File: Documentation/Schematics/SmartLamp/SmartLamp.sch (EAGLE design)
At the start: 31 parts, among them J1 POWER_JACKPTH_BREAD, J2 AVR_SPI_PROG_5X2PTH2, Q1 STN4NF03L, Q2 STN4NF03L, Q3 STN4NF03L, U1 MIC2920A, U2 DS3231MZ, U3 ATMEGA8/168/328, U4 HM-10

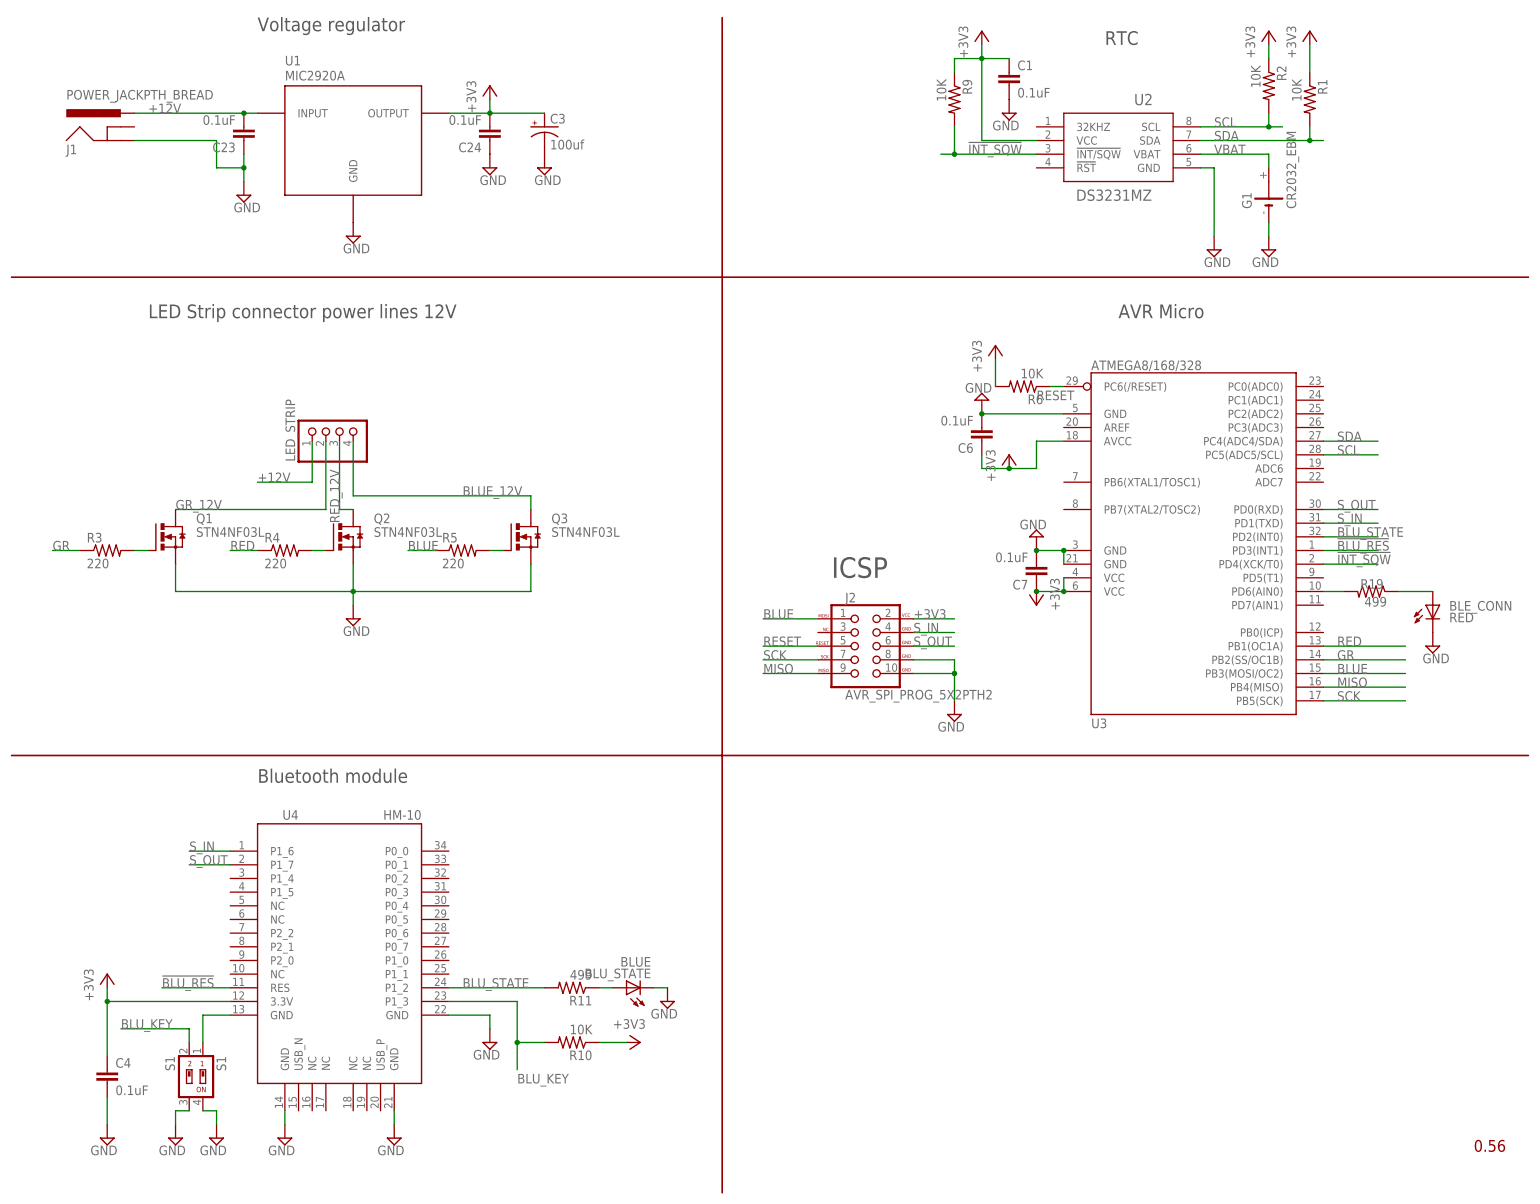
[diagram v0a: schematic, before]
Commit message: Arranged label with smashed part on schematic and board
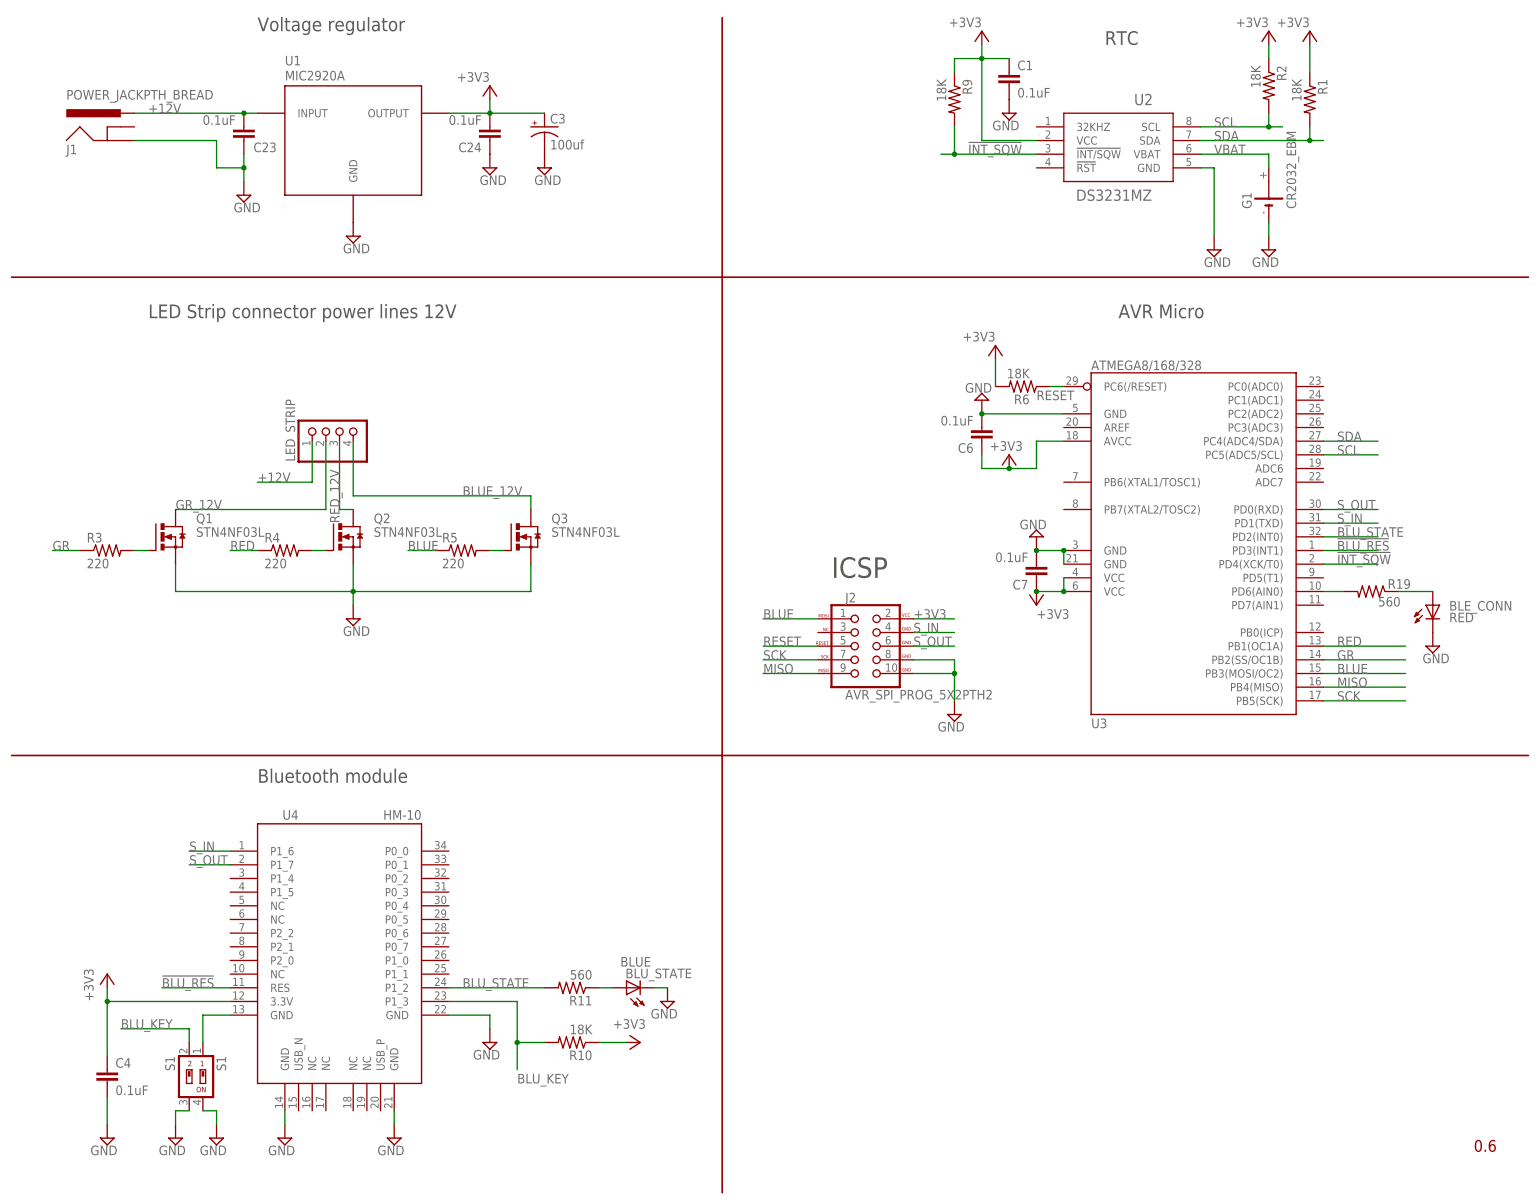
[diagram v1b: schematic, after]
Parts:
- R1, R10, R2, R6, R9: value 10K -> 18K
- R11, R19: value 499 -> 560
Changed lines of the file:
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@@
 <schematic xreflabel="%F%N/%S" xrefpart="/%S.%C%R">
 <attributes>
-<attribute name="VERSION" value="0.56"/>
+<attribute name="VERSION" value="0.6"/>
 </attributes>
 <variantdefs>
@@
 </classes>
 <parts>
-<part name="R2" library="rcl" deviceset="R-US_" device="R1206" value="10K"/>
-<part name="R1" library="rcl" deviceset="R-US_" device="R1206" value="10K"/>
+<part name="R2" library="rcl" deviceset="R-US_" device="R1206" value="18K"/>
+<part name="R1" library="rcl" deviceset="R-US_" device="R1206" value="18K"/>
 <part name="GND4" library="supply2" deviceset="GND" device=""/>
 <part name="J1" library="SparkFun-Connectors" deviceset="POWER_JACK" device="PTH_BREAD"/>
@@
 <part name="G1" library="CuSTOM_GB" deviceset="CR2032_EBM" device=""/>
 <part name="U2" library="Maxim_RTC" deviceset="DS3231MZ" device=""/>
-<part name="R9" library="rcl" deviceset="R-US_" device="R1206" value="10K"/>
+<part name="R9" library="rcl" deviceset="R-US_" device="R1206" value="18K"/>
 <part name="FRAME2" library="frames" deviceset="DOCFIELD" device=""/>
 <part name="SUPPLY52" library="supply2" deviceset="GND" device=""/>
@@
 <part name="Q2" library="transistor-power" deviceset="N-HEXFET-2D_?-*" device="SOT232" technology="IRLL014N" value="STN4NF03L"/>
 <part name="Q3" library="transistor-power" deviceset="N-HEXFET-2D_?-*" device="SOT232" technology="IRLL014N" value="STN4NF03L"/>
-<part name="R6" library="rcl" deviceset="R-US_" device="R1206" value="10K"/>
+<part name="R6" library="rcl" deviceset="R-US_" device="R1206" value="18K"/>
 <part name="+3V1" library="supply1" deviceset="+3V3" device=""/>
 <part name="C3" library="SparkFun-Capacitors" deviceset="CAP_POL" device="C" value="100uf"/>
@@
 <part name="SUPPLY20" library="supply2" deviceset="GND" device=""/>
 <part name="SUPPLY9" library="supply2" deviceset="GND" device=""/>
-<part name="R19" library="rcl" deviceset="R-US_" device="R1206" value="499"/>
+<part name="R19" library="rcl" deviceset="R-US_" device="R1206" value="560"/>
 <part name="SUPPLY10" library="supply2" deviceset="GND" device=""/>
 <part name="BLE_CONN" library="adafruit" deviceset="LED" device="CHIPLED_1206" value="RED"/>
 <part name="U4" library="HM-10_BLE" deviceset="HM-10" device=""/>
-<part name="R10" library="rcl" deviceset="R-US_" device="R1206" value="10K"/>
-<part name="R11" library="rcl" deviceset="R-US_" device="R1206" value="499"/>
+<part name="R10" library="rcl" deviceset="R-US_" device="R1206" value="18K"/>
+<part name="R11" library="rcl" deviceset="R-US_" device="R1206" value="560"/>
 <part name="BLU_STATE" library="adafruit" deviceset="LED" device="CHIPLED_1206" value="BLUE"/>
 <part name="GND7" library="supply2" deviceset="GND" device=""/>
@@
 <instance part="GND13" gate="GND" x="314.96" y="180.34" rot="MR0"/>
 <instance part="S1" gate="G$1" x="116.84" y="27.94" rot="R180"/>
-<instance part="+3V2" gate="G$1" x="261.62" y="220.98"/>
-<instance part="+3V3" gate="G$1" x="314.96" y="220.98"/>
-<instance part="+3V4" gate="G$1" x="322.58" y="220.98"/>
+<instance part="+3V2" gate="G$1" x="261.62" y="220.98" smashed="yes">
+<attribute name="VALUE" x="261.62" y="223.52" size="1.778" layer="96" rot="R180"/>
+</instance>
+<instance part="+3V3" gate="G$1" x="314.96" y="220.98" smashed="yes">
+<attribute name="VALUE" x="314.96" y="223.52" size="1.778" layer="96" rot="R180"/>
+</instance>
+<instance part="+3V4" gate="G$1" x="322.58" y="220.98" smashed="yes">
+<attribute name="VALUE" x="322.58" y="223.52" size="1.778" layer="96" rot="R180"/>
+</instance>
 <instance part="G1" gate="G$1" x="314.96" y="190.5" rot="R90"/>
 <instance part="U2" gate="A" x="287.02" y="200.66"/>
@@
 <instance part="FRAME2" gate="G$1" x="261.62" y="5.08"/>
 <instance part="SUPPLY52" gate="GND" x="124.46" y="190.5"/>
-<instance part="C23" gate="G$1" x="124.46" y="200.66" rot="R180"/>
+<instance part="C23" gate="G$1" x="124.46" y="200.66" smashed="yes" rot="R180">
+<attribute name="NAME" x="130.556" y="200.279" size="1.778" layer="95" rot="R180"/>
+<attribute name="VALUE" x="122.936" y="205.359" size="1.778" layer="96" rot="R180"/>
+</instance>
 <instance part="C24" gate="G$1" x="170.18" y="200.66" rot="R180"/>
 <instance part="SUPPLY54" gate="GND" x="170.18" y="195.58"/>
-<instance part="SUPPLY55" gate="G$1" x="170.18" y="210.82"/>
+<instance part="SUPPLY55" gate="G$1" x="170.18" y="210.82" smashed="yes">
+<attribute name="VALUE" x="170.18" y="213.36" size="1.778" layer="96" rot="R180"/>
+</instance>
 <instance part="SUPPLY7" gate="GND" x="304.8" y="180.34"/>
 <instance part="GND10" gate="GND" x="144.78" y="111.76"/>
@@
 <instance part="Q2" gate="G$1" x="142.24" y="127"/>
 <instance part="Q3" gate="G$1" x="175.26" y="127"/>
-<instance part="R6" gate="G$1" x="269.24" y="154.94" rot="R180"/>
-<instance part="+3V1" gate="G$1" x="264.16" y="162.56"/>
+<instance part="R6" gate="G$1" x="269.24" y="154.94" smashed="yes" rot="R180">
+<attribute name="NAME" x="270.51" y="153.4414" size="1.778" layer="95" rot="R180"/>
+<attribute name="VALUE" x="270.51" y="158.242" size="1.778" layer="96" rot="R180"/>
+</instance>
+<instance part="+3V1" gate="G$1" x="264.16" y="162.56" smashed="yes">
+<attribute name="VALUE" x="264.16" y="165.1" size="1.778" layer="96" rot="R180"/>
+</instance>
 <instance part="C3" gate="G$1" x="180.34" y="203.2"/>
 <instance part="SUPPLY8" gate="GND" x="180.34" y="195.58"/>
@@
 <instance part="SUPPLY9" gate="GND" x="271.78" y="127" rot="R180"/>
 <instance part="R19" gate="G$1" x="334.01" y="116.84" smashed="yes" rot="MR0">
-<attribute name="NAME" x="331.978" y="119.126" size="1.778" layer="95" rot="MR180"/>
-<attribute name="VALUE" x="332.74" y="115.824" size="1.778" layer="96" rot="MR180"/>
+<attribute name="NAME" x="337.058" y="119.126" size="1.778" layer="95" rot="MR180"/>
+<attribute name="VALUE" x="335.28" y="115.824" size="1.778" layer="96" rot="MR180"/>
 </instance>
 <instance part="SUPPLY10" gate="GND" x="345.44" y="106.68"/>
@@
 <instance part="U4" gate="G$1" x="142.24" y="45.72"/>
 <instance part="R10" gate="G$1" x="185.42" y="33.02" rot="R180"/>
-<instance part="R11" gate="G$1" x="185.42" y="43.18" rot="R180"/>
-<instance part="BLU_STATE" gate="G$1" x="195.58" y="43.18" rot="R90"/>
+<instance part="R11" gate="G$1" x="185.42" y="43.18" smashed="yes" rot="R180">
+<attribute name="NAME" x="189.23" y="41.6814" size="1.778" layer="95" rot="R180"/>
+<attribute name="VALUE" x="189.23" y="46.482" size="1.778" layer="96" rot="R180"/>
+</instance>
+<instance part="BLU_STATE" gate="G$1" x="195.58" y="43.18" smashed="yes" rot="R90">
+<attribute name="NAME" x="207.772" y="46.736" size="1.778" layer="95" rot="R180"/>
+<attribute name="VALUE" x="200.152" y="48.895" size="1.778" layer="96" rot="R180"/>
+</instance>
 <instance part="GND7" gate="GND" x="119.38" y="15.24" rot="MR0"/>
 <instance part="GND8" gate="GND" x="132.08" y="15.24" rot="MR0"/>
@@
 <instance part="GND2" gate="GND" x="111.76" y="15.24" rot="MR0"/>
 <instance part="GND3" gate="GND" x="99.06" y="15.24" rot="MR0"/>
-<instance part="+3V6" gate="G$1" x="266.7" y="142.24"/>
-<instance part="+3V8" gate="G$1" x="271.78" y="114.3" rot="R180"/>
+<instance part="+3V6" gate="G$1" x="266.7" y="142.24" smashed="yes">
+<attribute name="VALUE" x="269.24" y="144.78" size="1.778" layer="96" rot="R180"/>
+</instance>
+<instance part="+3V8" gate="G$1" x="271.78" y="114.3" smashed="yes" rot="R180">
+<attribute name="VALUE" x="271.78" y="111.76" size="1.778" layer="96"/>
+</instance>
 <instance part="C6" gate="G$1" x="261.62" y="144.78" rot="R180"/>
 <instance part="C7" gate="G$1" x="271.78" y="119.38" rot="R180"/>

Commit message: Schematic anb board v1.0: gerber file and png generated.
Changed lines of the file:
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@@
 <schematic xreflabel="%F%N/%S" xrefpart="/%S.%C%R">
 <attributes>
-<attribute name="VERSION" value="0.6"/>
+<attribute name="VERSION" value="1.0"/>
 </attributes>
 <variantdefs>
